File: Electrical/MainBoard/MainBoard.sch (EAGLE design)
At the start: 126 parts, among them IC1 MEGA1284-P, IC2 MCP4922-E/SL, IC3 MCP4921-E/SN, IC4 TL074D, IC5 TL074D, IC6 FT232RL, Q1 BC140-10, Q2 BC160, Q3 BC140-10, Q4 BC160, Q5 BD239, Q6 BD240, Q7 BC557, Q8 16MHz, X1 FH12-45S-0.5SH, X2 22-23-2021, X3 PN61729-S

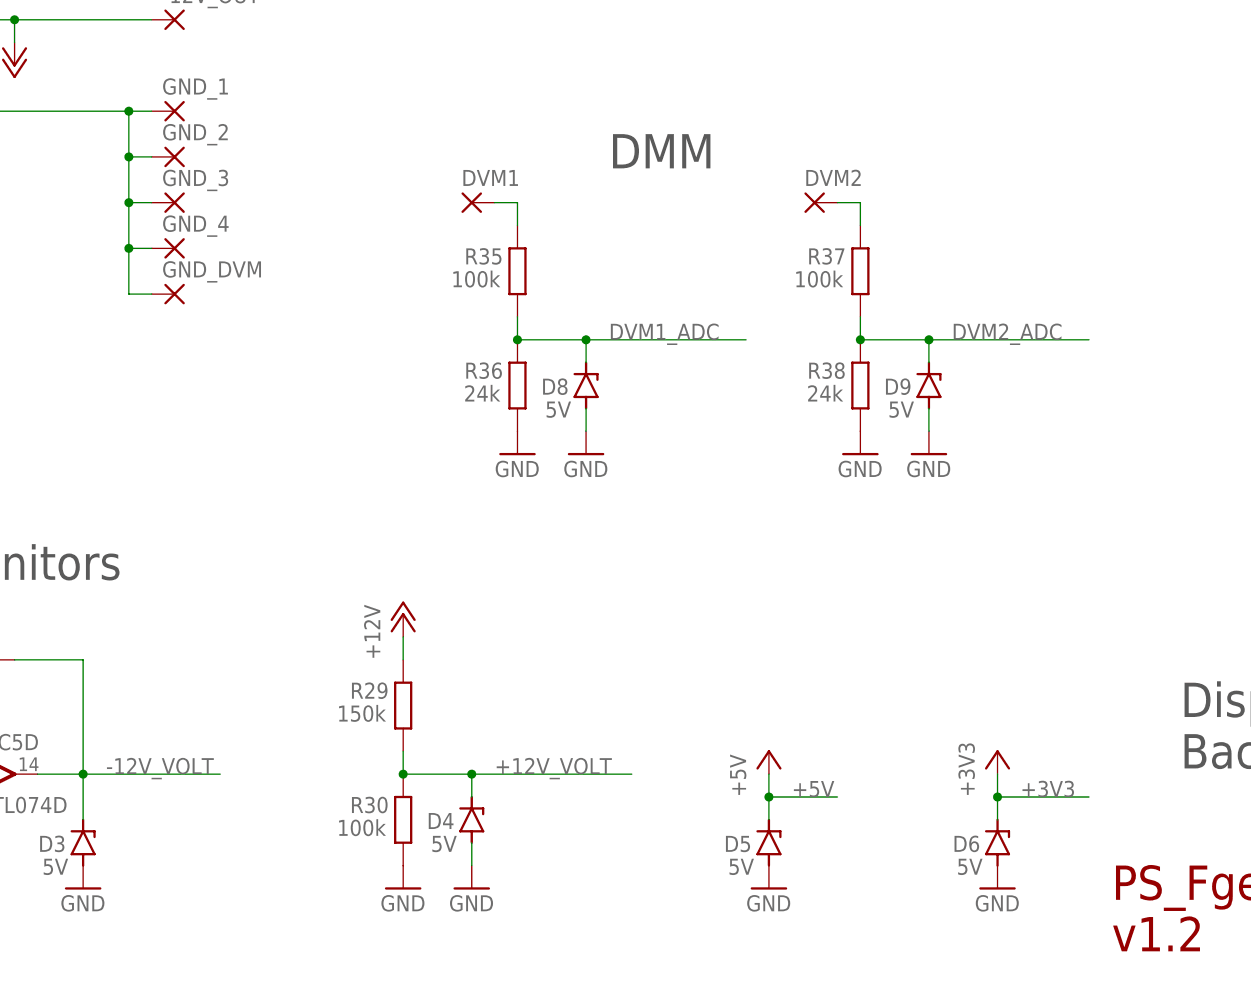
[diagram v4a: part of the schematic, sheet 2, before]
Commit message: Removed some Z-Diodes, removed Resistor R20 (PowerSupply, between OpAmp IC5B and transistors Q5 and Q6)
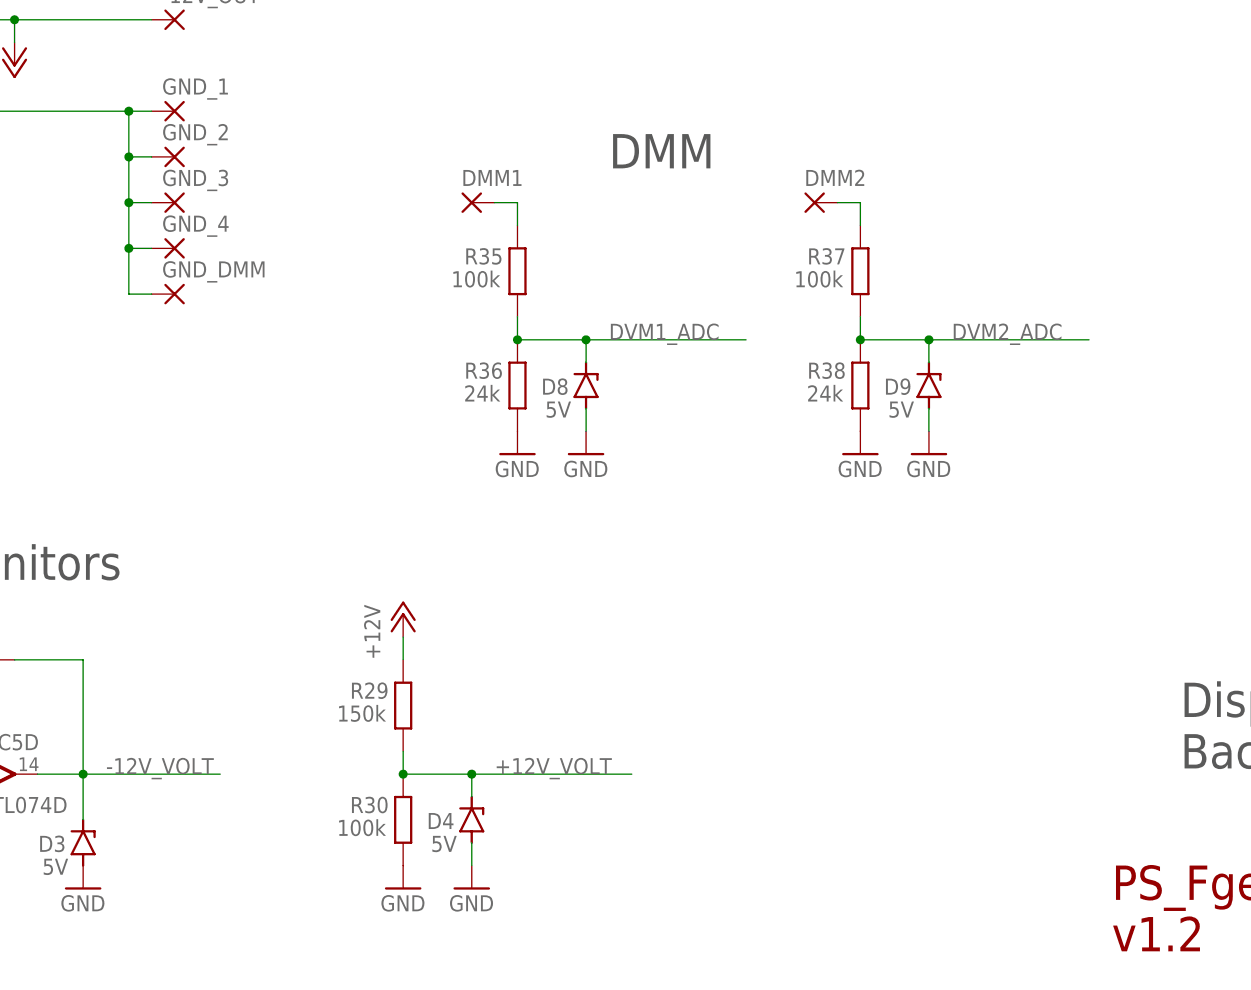
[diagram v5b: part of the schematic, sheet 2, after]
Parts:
- removed D5, D6, D7: 5V, diode:ZENER-DIODESOD80C
- removed R20: 100R, OwnDevices:R-EU_R0805
- renumbered DVM1 to DMM1, DVM2 to DMM2, GND_DVM to GND_DMM
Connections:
- net +3V3: no longer D6.C
- net +5V: no longer D5.C, D7.C
- net GND: no longer D5.A, D6.A, D7.A
- net N$18: no longer R20.2
- net N$20: no longer R20.1

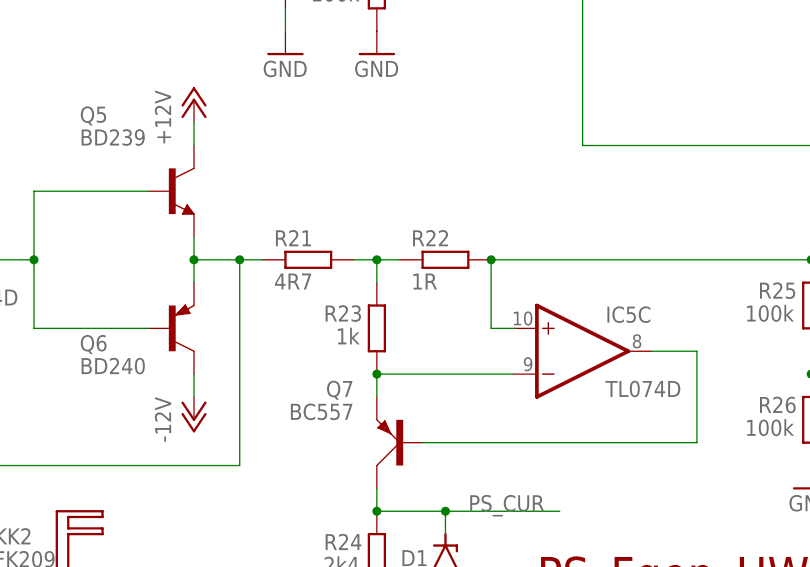
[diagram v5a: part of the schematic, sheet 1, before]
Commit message: Changed Resistor values of PowerSupply current measurement circuit (R21, R22, R23)
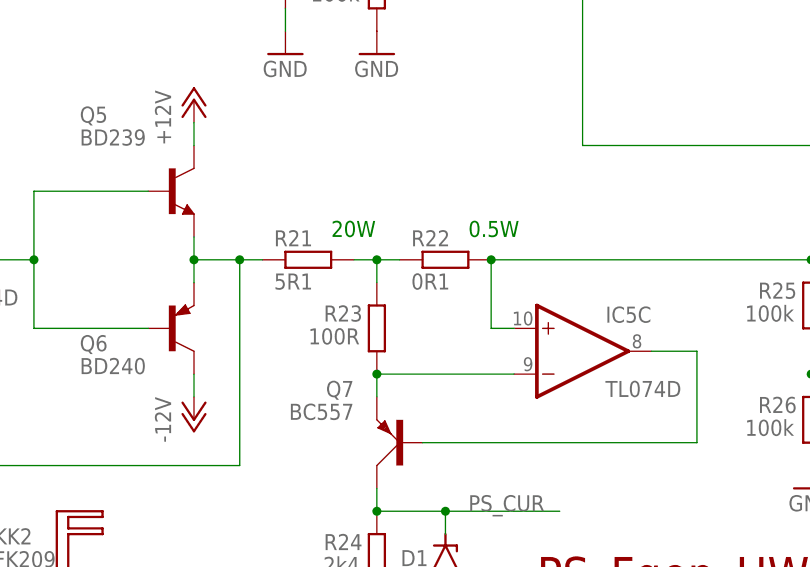
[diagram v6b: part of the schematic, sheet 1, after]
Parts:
- R21: value 4R7 -> 5R1
- R22: value 1R -> 0R1
- R23: value 1k -> 100R
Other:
- note added: "0.5W"
- note added: "20W"
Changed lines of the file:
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@@
 <part name="Q6" library="OwnDevices" library_urn="urn:adsk.eagle:library:19498084" deviceset="BD240" device="TO220BV" package3d_urn="urn:adsk.eagle:package:19394639/2" value="BD240"/>
 <part name="P-6" library="supply1" library_urn="urn:adsk.eagle:library:371" deviceset="-12V" device=""/>
-<part name="R21" library="OwnDevices" library_urn="urn:adsk.eagle:library:19498084" deviceset="R-EU_" device="0411/15" package3d_urn="urn:adsk.eagle:package:23568/2" value="4R7"/>
-<part name="R22" library="OwnDevices" library_urn="urn:adsk.eagle:library:19498084" deviceset="R-EU_" device="0411/15" package3d_urn="urn:adsk.eagle:package:23568/2" value="1R"/>
-<part name="R23" library="OwnDevices" library_urn="urn:adsk.eagle:library:19498084" deviceset="R-EU_" device="R0805" package3d_urn="urn:adsk.eagle:package:23553/2" value="1k"/>
+<part name="R21" library="OwnDevices" library_urn="urn:adsk.eagle:library:19498084" deviceset="R-EU_" device="0411/15" package3d_urn="urn:adsk.eagle:package:23568/2" value="5R1"/>
+<part name="R22" library="OwnDevices" library_urn="urn:adsk.eagle:library:19498084" deviceset="R-EU_" device="0411/15" package3d_urn="urn:adsk.eagle:package:23568/2" value="0R1"/>
+<part name="R23" library="OwnDevices" library_urn="urn:adsk.eagle:library:19498084" deviceset="R-EU_" device="R0805" package3d_urn="urn:adsk.eagle:package:23553/2" value="100R"/>
 <part name="R24" library="OwnDevices" library_urn="urn:adsk.eagle:library:19498084" deviceset="R-EU_" device="R0805" package3d_urn="urn:adsk.eagle:package:23553/2" value="2k4"/>
 <part name="Q7" library="transistor-small-signal" library_urn="urn:adsk.eagle:library:401" deviceset="BC557" device="" package3d_urn="urn:adsk.eagle:package:29732/3"/>
@@
 <text x="50.8" y="134.62" size="3.81" layer="97">DDS1 / DDS2</text>
 <text x="7.62" y="63.5" size="3.81" layer="97">Power Supply</text>
+<text x="154.94" y="58.42" size="1.778" layer="91">0.5W</text>
+<text x="139.7" y="58.42" size="1.778" layer="91">20W</text>
 </plain>
 <instances>

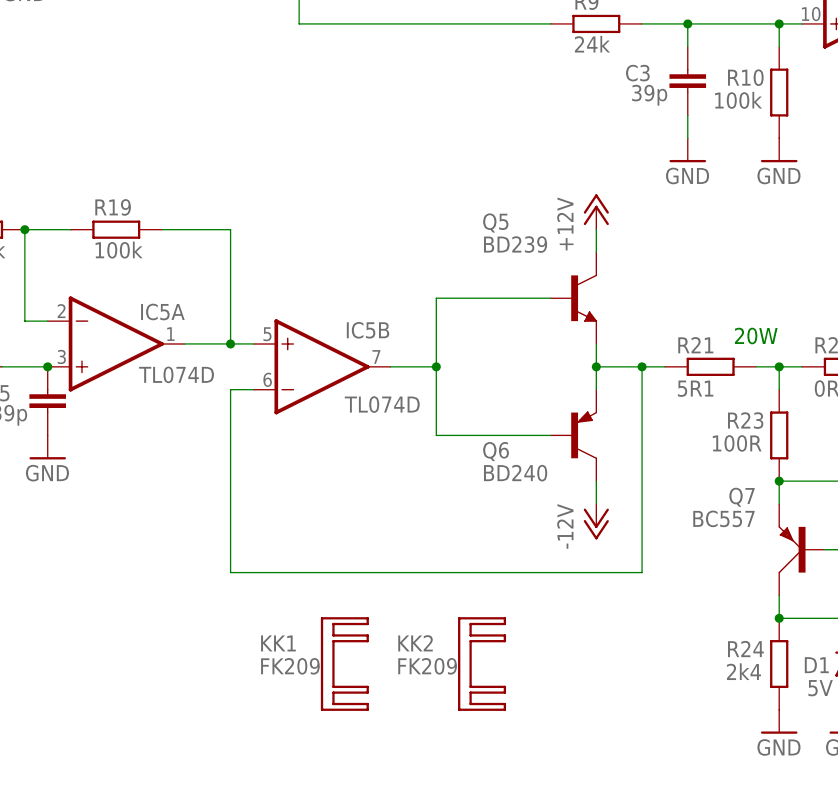
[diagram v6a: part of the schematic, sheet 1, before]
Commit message: Changed power stage of PowerSupply channel
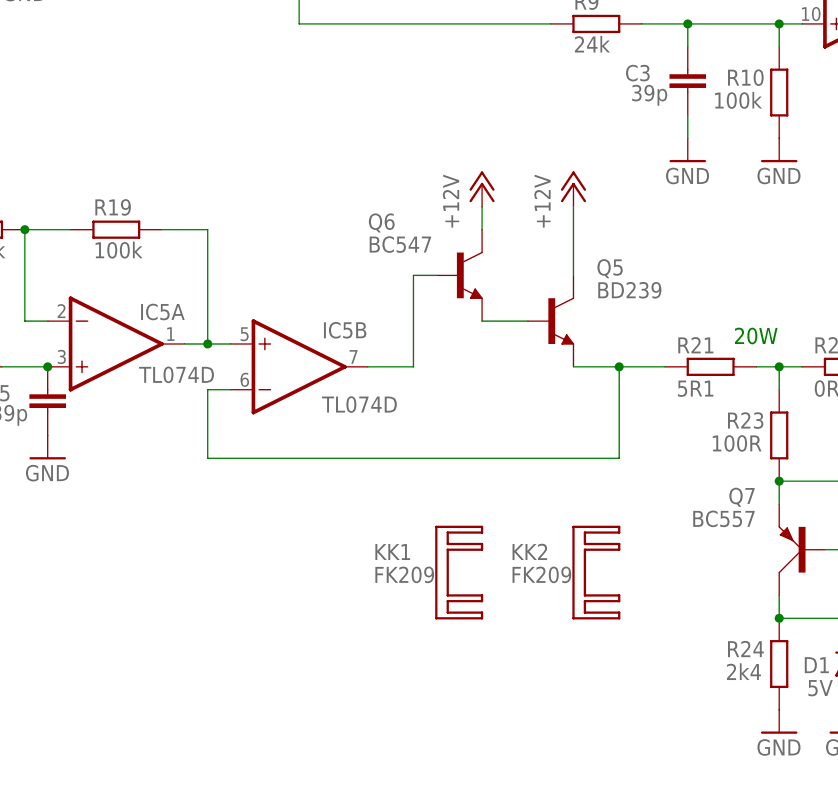
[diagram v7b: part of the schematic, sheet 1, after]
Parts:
- Q6: value BD240 -> BC547; device OwnDevices:BD240TO220BV -> transistor:BC547
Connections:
- new net N$38: IC5B.OUT, Q6.B
- net +12V: now also Q6.C
- net -12V: no longer Q6.C
- net N$18: no longer Q6.E
- net N$20: now also Q6.E; no longer IC5B.OUT, Q6.B
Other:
- moved on the sheet: IC5B, KK1, KK2, Q5
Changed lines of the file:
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@@
 <part name="Q5" library="OwnDevices" library_urn="urn:adsk.eagle:library:19498084" deviceset="BD239*" device="TO220BV" package3d_urn="urn:adsk.eagle:package:19394639/2" value="BD239"/>
 <part name="P+12" library="supply1" library_urn="urn:adsk.eagle:library:371" deviceset="+12V" device=""/>
-<part name="Q6" library="OwnDevices" library_urn="urn:adsk.eagle:library:19498084" deviceset="BD240" device="TO220BV" package3d_urn="urn:adsk.eagle:package:19394639/2" value="BD240"/>
-<part name="P-6" library="supply1" library_urn="urn:adsk.eagle:library:371" deviceset="-12V" device=""/>
 <part name="R21" library="OwnDevices" library_urn="urn:adsk.eagle:library:19498084" deviceset="R-EU_" device="0411/15" package3d_urn="urn:adsk.eagle:package:23568/2" value="5R1"/>
 <part name="R22" library="OwnDevices" library_urn="urn:adsk.eagle:library:19498084" deviceset="R-EU_" device="0411/15" package3d_urn="urn:adsk.eagle:package:23568/2" value="0R1"/>
@@
 <part name="P+23" library="supply1" library_urn="urn:adsk.eagle:library:371" deviceset="+5V" device=""/>
 <part name="P+20" library="supply1" library_urn="urn:adsk.eagle:library:371" deviceset="+5V" device=""/>
+<part name="Q6" library="transistor" library_urn="urn:adsk.eagle:library:402" deviceset="BC547" device="" package3d_urn="urn:adsk.eagle:package:28523/2"/>
+<part name="P+15" library="supply1" library_urn="urn:adsk.eagle:library:371" deviceset="+12V" device=""/>
 </parts>
 <sheets>
@@
 <attribute name="VALUE" x="73.66" y="55.88" size="1.778" layer="96" rot="MR180"/>
 </instance>
-<instance part="IC5" gate="B" x="93.98" y="55.88" smashed="yes">
-<attribute name="NAME" x="96.52" y="59.055" size="1.778" layer="95"/>
-<attribute name="VALUE" x="96.52" y="50.8" size="1.778" layer="96"/>
+<instance part="IC5" gate="B" x="91.44" y="55.88" smashed="yes">
+<attribute name="NAME" x="93.98" y="59.055" size="1.778" layer="95"/>
+<attribute name="VALUE" x="93.98" y="50.8" size="1.778" layer="96"/>
 </instance>
 <instance part="IC5" gate="C" x="167.64" y="45.72" smashed="yes">
@@
 <attribute name="VALUE" x="45.72" y="66.04" size="1.778" layer="96"/>
 </instance>
-<instance part="Q5" gate="G$1" x="121.92" y="63.5" smashed="yes">
-<attribute name="NAME" x="111.76" y="71.12" size="1.778" layer="95"/>
-<attribute name="VALUE" x="111.76" y="68.58" size="1.778" layer="96"/>
-</instance>
-<instance part="P+12" gate="1" x="124.46" y="73.66" smashed="yes">
-<attribute name="VALUE" x="121.92" y="68.58" size="1.778" layer="96" rot="R90"/>
-</instance>
-<instance part="Q6" gate="G$1" x="121.92" y="48.26" smashed="yes">
-<attribute name="NAME" x="111.76" y="45.72" size="1.778" layer="95"/>
-<attribute name="VALUE" x="111.76" y="43.18" size="1.778" layer="96"/>
-</instance>
-<instance part="P-6" gate="1" x="124.46" y="38.1" smashed="yes">
-<attribute name="VALUE" x="121.92" y="35.56" size="1.778" layer="96" rot="R90"/>
+<instance part="Q5" gate="G$1" x="119.38" y="60.96" smashed="yes">
+<attribute name="NAME" x="124.46" y="66.04" size="1.778" layer="95"/>
+<attribute name="VALUE" x="124.46" y="63.5" size="1.778" layer="96"/>
+</instance>
+<instance part="P+12" gate="1" x="121.92" y="76.2" smashed="yes">
+<attribute name="VALUE" x="119.38" y="71.12" size="1.778" layer="96" rot="R90"/>
 </instance>
 <instance part="R21" gate="G$1" x="137.16" y="55.88" smashed="yes">
@@
 <attribute name="VALUE" x="220.98" y="27.94" size="1.778" layer="96"/>
 </instance>
-<instance part="KK1" gate="G$1" x="93.98" y="22.86" smashed="yes" rot="MR90">
-<attribute name="NAME" x="86.995" y="26.035" size="1.778" layer="95" rot="MR180"/>
-<attribute name="VALUE" x="86.995" y="23.495" size="1.778" layer="96" rot="MR180"/>
-</instance>
-<instance part="KK2" gate="G$1" x="109.22" y="22.86" smashed="yes" rot="MR90">
-<attribute name="NAME" x="102.235" y="26.035" size="1.778" layer="95" rot="MR180"/>
-<attribute name="VALUE" x="102.235" y="23.495" size="1.778" layer="96" rot="MR180"/>
+<instance part="KK1" gate="G$1" x="106.68" y="33.02" smashed="yes" rot="MR90">
+<attribute name="NAME" x="99.695" y="36.195" size="1.778" layer="95" rot="MR180"/>
+<attribute name="VALUE" x="99.695" y="33.655" size="1.778" layer="96" rot="MR180"/>
+</instance>
+<instance part="KK2" gate="G$1" x="121.92" y="33.02" smashed="yes" rot="MR90">
+<attribute name="NAME" x="114.935" y="36.195" size="1.778" layer="95" rot="MR180"/>
+<attribute name="VALUE" x="114.935" y="33.655" size="1.778" layer="96" rot="MR180"/>
 </instance>
 <instance part="U$3" gate="G$1" x="213.36" y="154.94" smashed="yes">
@@
 <attribute name="NAME" x="232.41" y="101.6" size="1.778" layer="95"/>
 <attribute name="VALUE" x="229.743" y="99.06" size="1.778" layer="96"/>
+</instance>
+<instance part="Q6" gate="G$1" x="109.22" y="66.04" smashed="yes">
+<attribute name="NAME" x="99.06" y="71.12" size="1.778" layer="95"/>
+<attribute name="VALUE" x="99.06" y="68.58" size="1.778" layer="96"/>
+</instance>
+<instance part="P+15" gate="1" x="111.76" y="76.2" smashed="yes">
+<attribute name="VALUE" x="109.22" y="71.12" size="1.778" layer="96" rot="R90"/>
 </instance>
 </instances>
@@
 <pinref part="Q5" gate="G$1" pin="C"/>
 <pinref part="P+12" gate="1" pin="+12V"/>
-<wire x1="124.46" y1="68.58" x2="124.46" y2="71.12" width="0.1524" layer="91"/>
+<wire x1="121.92" y1="66.04" x2="121.92" y2="73.66" width="0.1524" layer="91"/>
+</segment>
+<segment>
+<pinref part="Q6" gate="G$1" pin="C"/>
+<pinref part="P+15" gate="1" pin="+12V"/>
+<wire x1="111.76" y1="71.12" x2="111.76" y2="73.66" width="0.1524" layer="91"/>
 </segment>
 </net>
@@
 <pinref part="P-5" gate="1" pin="-12V"/>
 <wire x1="205.74" y1="81.28" x2="205.74" y2="76.2" width="0.1524" layer="91"/>
-</segment>
-<segment>
-<pinref part="P-6" gate="1" pin="-12V"/>
-<pinref part="Q6" gate="G$1" pin="C"/>
-<wire x1="124.46" y1="40.64" x2="124.46" y2="43.18" width="0.1524" layer="91"/>
 </segment>
 </net>
@@
 <segment>
 <pinref part="R19" gate="G$1" pin="2"/>
-<wire x1="76.2" y1="71.12" x2="83.82" y2="71.12" width="0.1524" layer="91"/>
+<wire x1="76.2" y1="71.12" x2="81.28" y2="71.12" width="0.1524" layer="91"/>
 <pinref part="IC5" gate="A" pin="OUT"/>
-<wire x1="83.82" y1="71.12" x2="83.82" y2="58.42" width="0.1524" layer="91"/>
-<wire x1="83.82" y1="58.42" x2="78.74" y2="58.42" width="0.1524" layer="91"/>
+<wire x1="81.28" y1="71.12" x2="81.28" y2="58.42" width="0.1524" layer="91"/>
+<wire x1="81.28" y1="58.42" x2="78.74" y2="58.42" width="0.1524" layer="91"/>
 <pinref part="IC5" gate="B" pin="+IN"/>
-<wire x1="86.36" y1="58.42" x2="83.82" y2="58.42" width="0.1524" layer="91"/>
-<junction x="83.82" y="58.42"/>
+<wire x1="83.82" y1="58.42" x2="81.28" y2="58.42" width="0.1524" layer="91"/>
+<junction x="81.28" y="58.42"/>
 </segment>
 </net>
 <net name="N$18" class="0">
 <segment>
+<pinref part="Q5" gate="G$1" pin="E"/>
+<pinref part="IC5" gate="B" pin="-IN"/>
+<wire x1="83.82" y1="53.34" x2="81.28" y2="53.34" width="0.1524" layer="91"/>
+<wire x1="81.28" y1="53.34" x2="81.28" y2="45.72" width="0.1524" layer="91"/>
+<wire x1="81.28" y1="45.72" x2="127" y2="45.72" width="0.1524" layer="91"/>
+<wire x1="127" y1="45.72" x2="127" y2="55.88" width="0.1524" layer="91"/>
+<wire x1="127" y1="55.88" x2="121.92" y2="55.88" width="0.1524" layer="91"/>
+<pinref part="R21" gate="G$1" pin="1"/>
+<wire x1="132.08" y1="55.88" x2="127" y2="55.88" width="0.1524" layer="91"/>
+<junction x="127" y="55.88"/>
+</segment>
+</net>
+<net name="N$20" class="0">
+<segment>
+<pinref part="Q5" gate="G$1" pin="B"/>
+<wire x1="116.84" y1="60.96" x2="111.76" y2="60.96" width="0.1524" layer="91"/>
 <pinref part="Q6" gate="G$1" pin="E"/>
-<pinref part="Q5" gate="G$1" pin="E"/>
-<wire x1="124.46" y1="53.34" x2="124.46" y2="55.88" width="0.1524" layer="91"/>
-<wire x1="124.46" y1="55.88" x2="124.46" y2="58.42" width="0.1524" layer="91"/>
-<junction x="124.46" y="55.88"/>
-<pinref part="IC5" gate="B" pin="-IN"/>
-<wire x1="86.36" y1="53.34" x2="83.82" y2="53.34" width="0.1524" layer="91"/>
-<wire x1="83.82" y1="53.34" x2="83.82" y2="33.02" width="0.1524" layer="91"/>
-<wire x1="83.82" y1="33.02" x2="129.54" y2="33.02" width="0.1524" layer="91"/>
-<wire x1="129.54" y1="33.02" x2="129.54" y2="55.88" width="0.1524" layer="91"/>
-<wire x1="129.54" y1="55.88" x2="124.46" y2="55.88" width="0.1524" layer="91"/>
-<pinref part="R21" gate="G$1" pin="1"/>
-<wire x1="132.08" y1="55.88" x2="129.54" y2="55.88" width="0.1524" layer="91"/>
-<junction x="129.54" y="55.88"/>
-</segment>
-</net>
-<net name="N$20" class="0">
-<segment>
-<pinref part="Q5" gate="G$1" pin="B"/>
-<wire x1="119.38" y1="63.5" x2="106.68" y2="63.5" width="0.1524" layer="91"/>
-<pinref part="Q6" gate="G$1" pin="B"/>
-<wire x1="106.68" y1="63.5" x2="106.68" y2="55.88" width="0.1524" layer="91"/>
-<wire x1="106.68" y1="55.88" x2="106.68" y2="48.26" width="0.1524" layer="91"/>
-<wire x1="106.68" y1="48.26" x2="119.38" y2="48.26" width="0.1524" layer="91"/>
-<junction x="106.68" y="55.88"/>
-<pinref part="IC5" gate="B" pin="OUT"/>
-<wire x1="101.6" y1="55.88" x2="106.68" y2="55.88" width="0.1524" layer="91"/>
 </segment>
 </net>
@@
 </segment>
 </net>
+<net name="N$38" class="0">
+<segment>
+<pinref part="IC5" gate="B" pin="OUT"/>
+<wire x1="99.06" y1="55.88" x2="104.14" y2="55.88" width="0.1524" layer="91"/>
+<wire x1="104.14" y1="55.88" x2="104.14" y2="66.04" width="0.1524" layer="91"/>
+<pinref part="Q6" gate="G$1" pin="B"/>
+<wire x1="104.14" y1="66.04" x2="106.68" y2="66.04" width="0.1524" layer="91"/>
+</segment>
+</net>
